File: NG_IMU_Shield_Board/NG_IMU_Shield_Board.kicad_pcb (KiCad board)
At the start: 2 copper layers, 87.6 x 45.7 mm, 21 parts, among them J1 Conn_01x04_Female, J2 Conn_01x02_Male, J3 Conn_01x10_Female, J4 Conn_01x03_Female, J6 Conn_01x11_Male, U1 SN75ALS175, U2 Level_Converter, U3 Teensy_v4.0

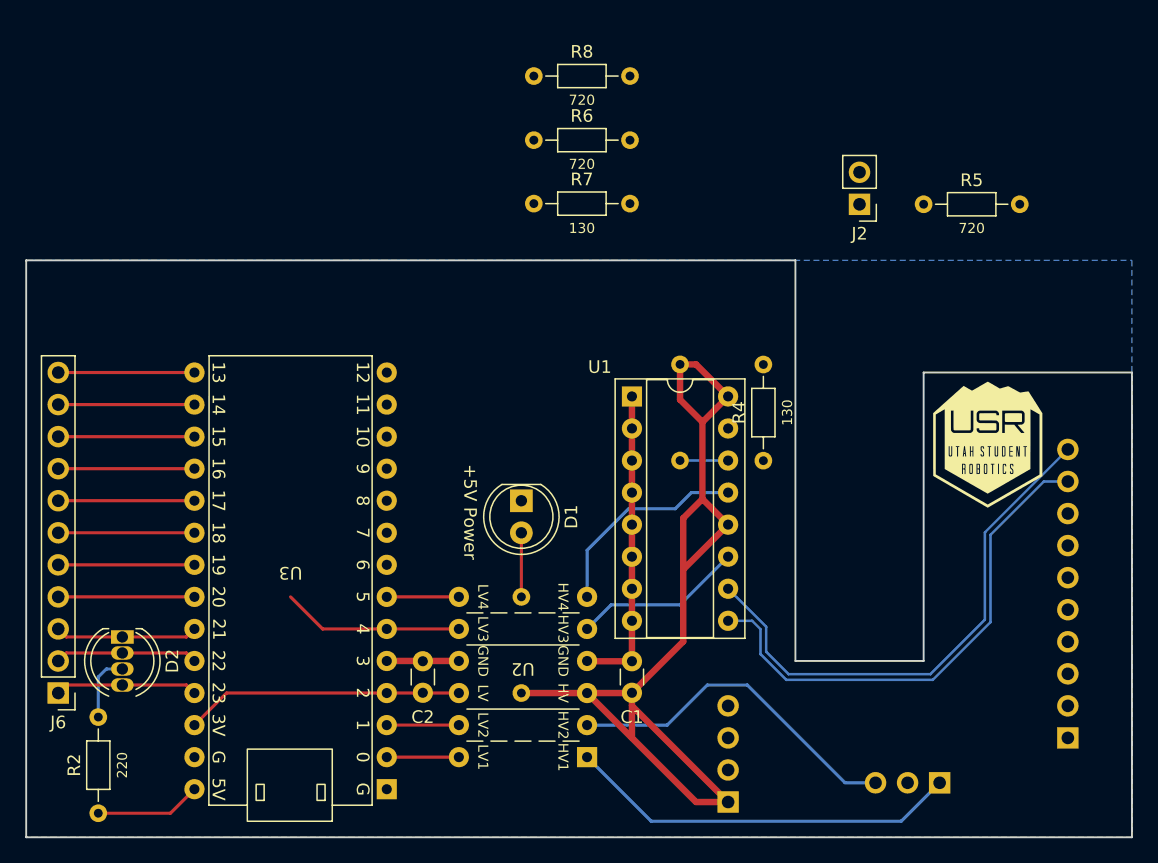
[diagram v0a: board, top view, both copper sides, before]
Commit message: Changed to use LM393 and completed schematic
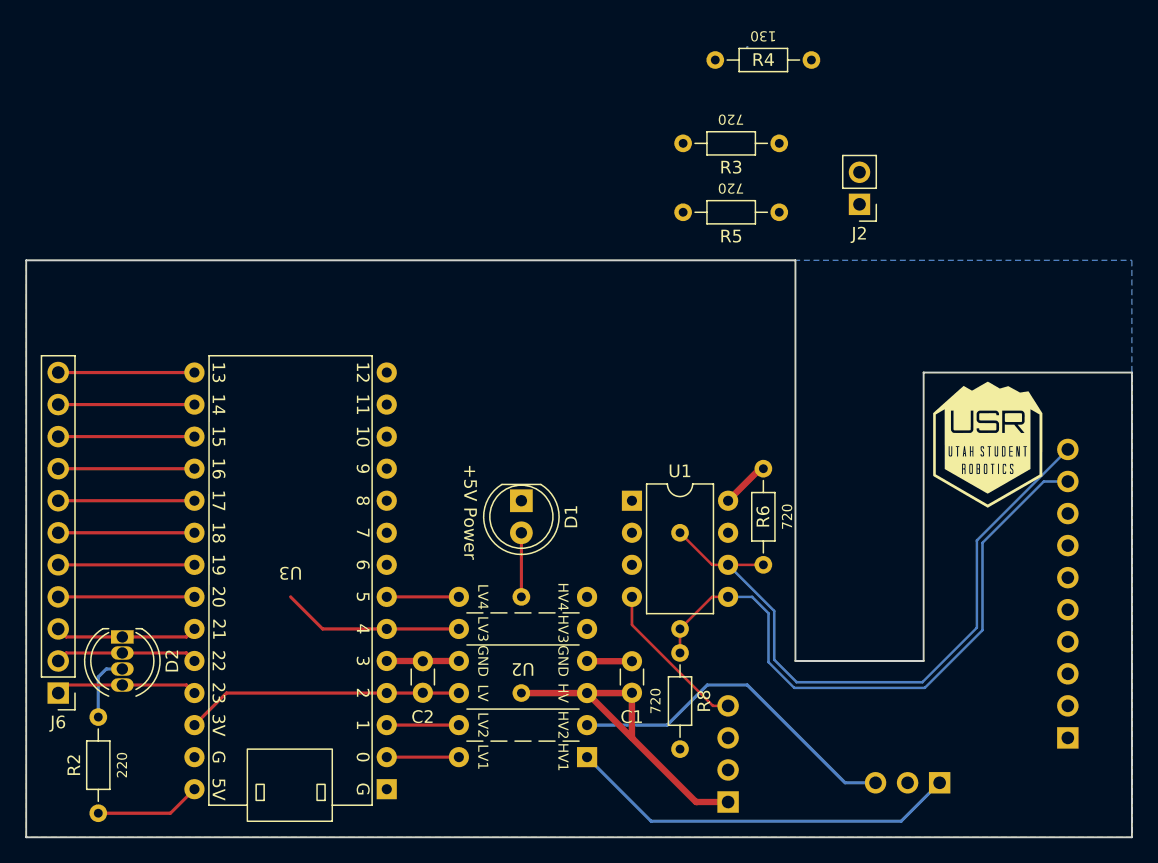
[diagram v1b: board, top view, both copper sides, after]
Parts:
- R3: moved to F.Cu
- R7: moved to B.Cu
- U1: value SN75ALS175 -> LM393; footprint Package_DIP:DIP-16_W7.62mm_Socket -> Package_DIP:DIP-8_W7.62mm
- moved R8 47.2 mm to (157.2, 89.5), turned to -90 degrees
- moved R4 32.0 mm to (167.6, 42.5), turned to 180 degrees
- moved R6 31.8 mm to (163.8, 74.9), turned to -90 degrees
- moved R7 28.5 mm to (157.2, 80.0), turned to -90 degrees
- moved R5 26.7 mm to (157.5, 54.6), turned to 0 degrees
- moved R3 19.2 mm to (165.1, 49.1), turned to 180 degrees
- moved U1 8.27 mm to (153.4, 77.5)
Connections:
- U1 pad 1: /0V -> /Test_clean
- U1 pad 2: /0V -> /Test+
- U1 pad 3: /0V -> /Test-
- U1 pad 4: /0V -> /-15V
- U1 pad 5: /0V -> /Ready-
- U1 pad 6: /0V -> /Ready+
- U1 pad 7: /0V -> /Ready_clean
- U1 pad 8: /0V -> /+5V
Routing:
- net /+5V: track 82.6 -> 30.9 mm
- net /0V: track 30.2 -> 9.25 mm
- net /Test_clean: track 16.8 -> 0.00 mm
- net /Ready_clean: track 13.5 -> 0.00 mm
- net /-15V: track 0.00 -> 12.5 mm
- net /Ready+: track 42.3 -> 52.4 mm
- net /Ready-: track 40.6 -> 49.8 mm
- net /Test+: track 3.81 -> 0.00 mm
